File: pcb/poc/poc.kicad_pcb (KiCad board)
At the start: 2 copper layers, 100 x 100 mm, 63 parts, among them J1 USB_B_Mini, J2 Right, J3 Left, J4 AVR-ISP-6, J5 Conn_02x08_Odd_Even, J6 Conn_02x08_Odd_Even, J7 Conn_01x02, J8 Conn_01x02, J9 Conn_02x02_Odd_Even, SW1 SW_Push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

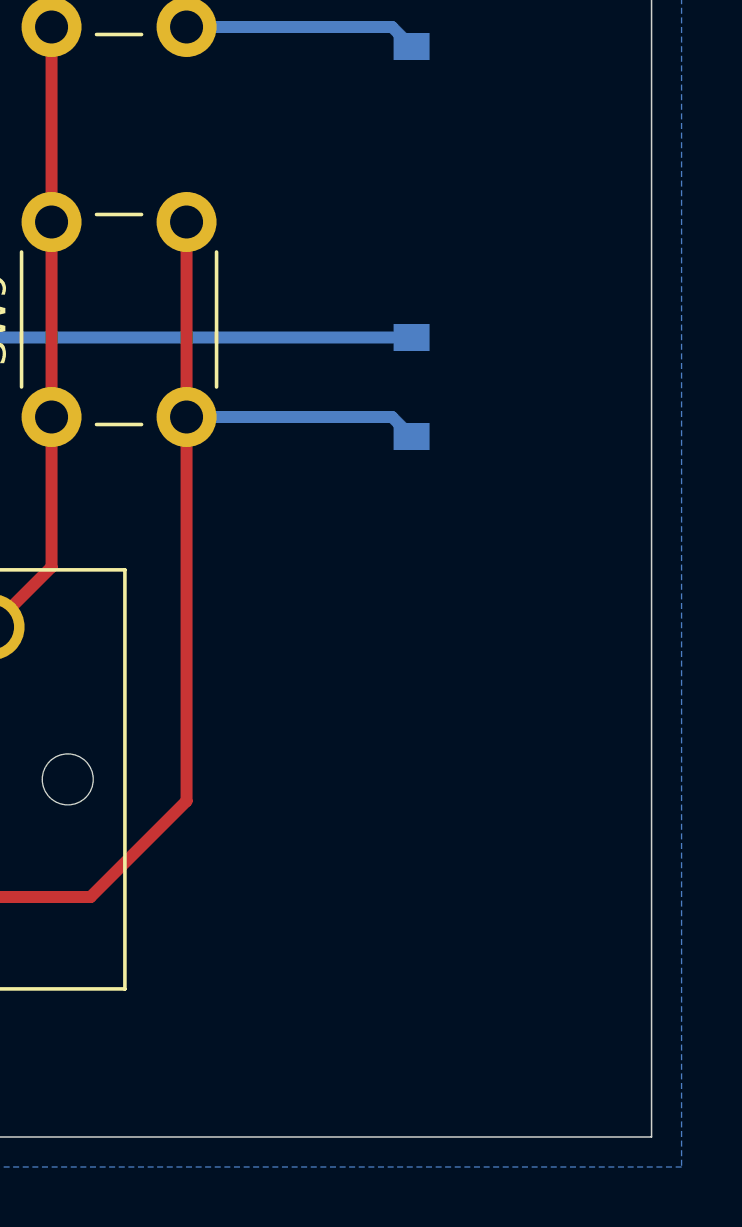
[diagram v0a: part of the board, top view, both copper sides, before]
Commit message: pcb: poc: Sign the PCB
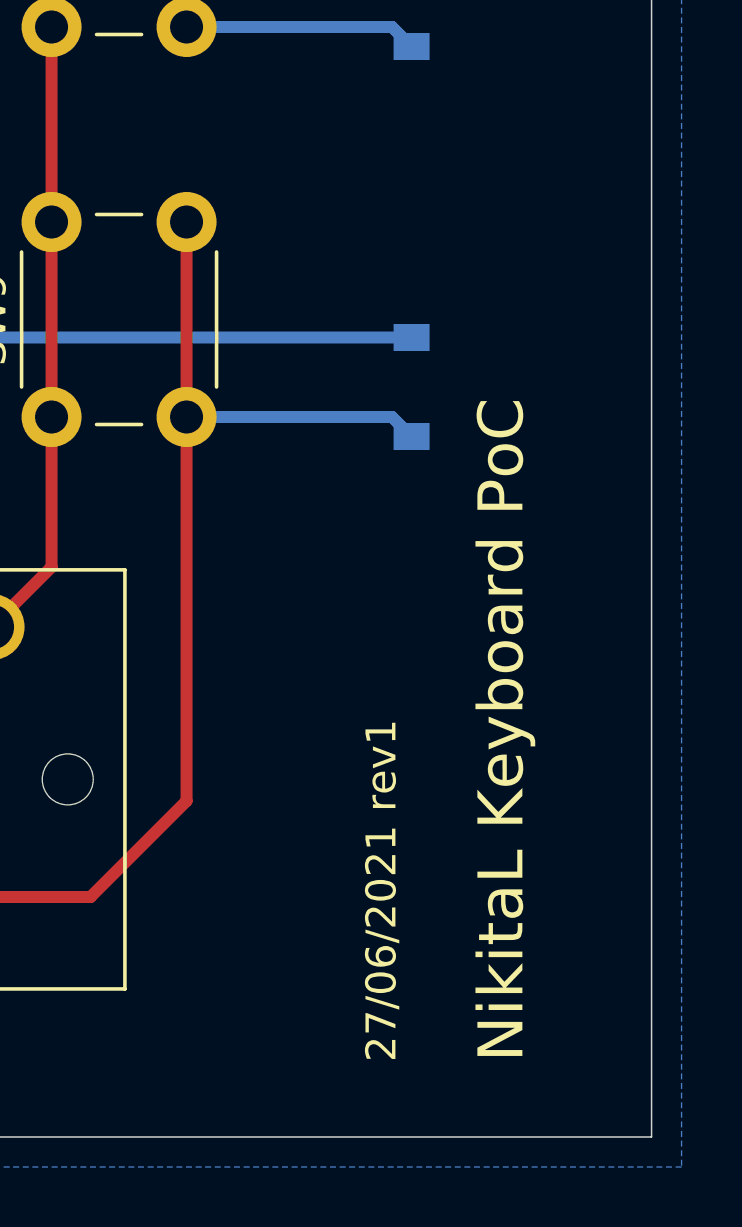
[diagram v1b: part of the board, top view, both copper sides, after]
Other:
- board text added: "27/06/2021 rev1"
- board text added: "NikitaL Keyboard PoC"
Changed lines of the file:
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@@
   (general
     (thickness 1.6)
-    (drawings 48)
+    (drawings 50)
     (tracks 775)
     (zones 0)
@@
     )
   )
+  (gr_text "27/06/2021 rev1" (at 161 152.5 90) (layer F.SilkS)
+    (effects (font (size 1 1) (thickness 0.15)) (justify left))
+  )
+  (gr_text "NikitaL Keyboard PoC" (at 165 152.5 90) (layer F.SilkS)
+    (effects (font (size 1.5 1.5) (thickness 0.3)) (justify left))
+  )
   (gr_text COL1 (at 97.5 148.5) (layer F.SilkS)
